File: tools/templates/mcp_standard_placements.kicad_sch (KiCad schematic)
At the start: 150 parts, among them J1 ICSP, J3 PIR BOARD, J5 MOTOR, J6 DNP, Q1 FMOS3401A?, Q11 MMBTA55?, Q2 BC847B?, Q3 MMBTA55?, Q4 MMBTA55?, Q5 MMBTA55?, Q6 MMBTA55?, Q7 BC857C?, Q8 N/P pair? (372A), Q9 DNP, U1 S-1200B45? [pins], U106 U6A / DNP, U2 SN74LVC2G14DBV?, U3 SGM8542XS, U4 PIC16F18855, U5 MX512H, U6 S-812C33AMC? / 3.3V, U7 DNP, Y1 20 MHz

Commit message: Record measured D3 rails and R42 continuity; close V082 association
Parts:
- D3: PhysicalConnectionEvidence (none) -> 2026-10-09 user meter report: D3.L=GND; D3.R=VDD TP via V08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
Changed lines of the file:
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@@
 				) hide)
 		)
+    (property "PhysicalConnectionEvidence" "2026-10-09 user meter report: D3.L=GND; D3.R=VDD TP via V082. D3.S to R42=1.2 ohm; resistor end not explicitly named. Photo selects R42.2 nearest D3; other end already mapped to TP4/PIC25. Fitted BAV99 identity and signal function remain candidates." (at 556.26 233.68 0)
+      (effects (font (size 1.27 1.27)) (hide yes))
+    )
 	)
 	(symbol

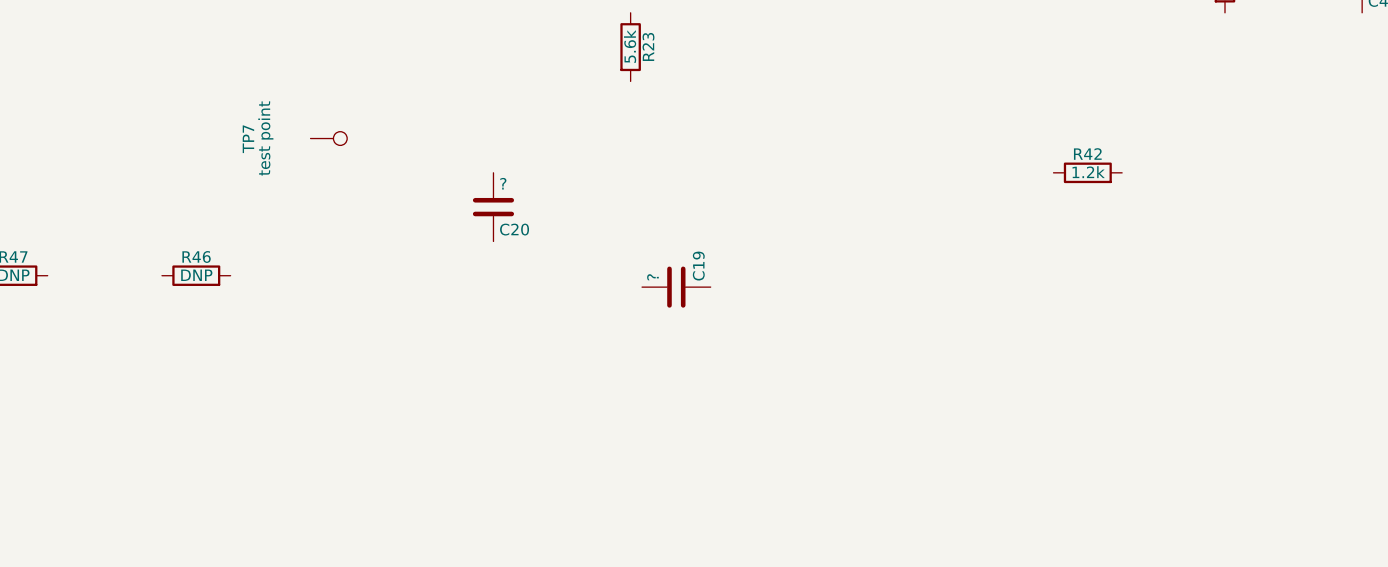
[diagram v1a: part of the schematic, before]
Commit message: Map D2 antenna and receiver connections with empty R46 option
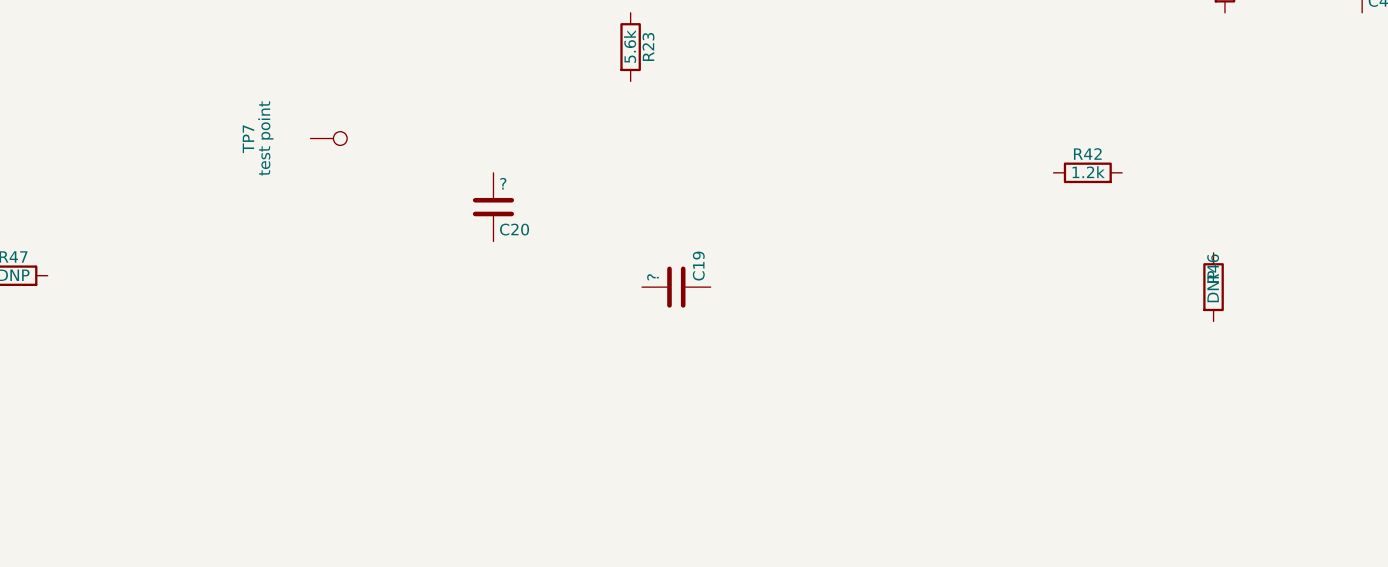
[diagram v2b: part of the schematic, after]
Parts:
- D2: MeasurementEvidence (none) -> User: R (upper-left)-C20 lower = 1 ohm; L (upper-right)-ANT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
- R46: MeasurementEvidence (none) -> User confirms empty R46 footprint: upper pad/model1 joins D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
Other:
- moved on the sheet: R46
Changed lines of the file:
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@@
 			)
 		)
-    (property "PhysicalPinEvidence" "IMG_2437 front: CLK-DAT-GND-VDD-VPP left to right; square pad is VPP/right end. IMG_2439 rear corroborates square end. Native pin1=VPP,2=VDD,3=GND,4=DAT,5=CLK; photo-based physical order, not new electrical measurements." (at 344.17 59.69 0)
-      (effects (font (size 1.27 1.27)) (hide yes))
-    )
+		(property "PhysicalPinEvidence" "IMG_2437 front: CLK-DAT-GND-VDD-VPP left to right; square pad is VPP/right end. IMG_2439 rear corroborates square end. Native pin1=VPP,2=VDD,3=GND,4=DAT,5=CLK; photo-based physical order, not new electrical measurements."
+			(at 344.17 59.69 0)
+			(effects
+				(font
+					(size 1.27 1.27)
+				)
+				(hide yes)
+			)
+		)
 		(pin "1"
 		)
@@
 	(symbol
 		(lib_id "Device:R")
-		(at 412.75 248.92 90)
+		(at 525.78 250.19 0)
 		(unit 1)
 		(body_style 1)
@@
 		(dnp no)
 		(property "Reference" "R46"
-			(at 412.75 246.888 90)
+			(at 525.78 248.15800000000002 90)
 			(show_name no)
 			(do_not_autoplace no)
@@
 		)
 		(property "Value" "DNP"
-			(at 412.75 248.92 90)
+			(at 525.78 250.19 90)
 			(show_name no)
 			(do_not_autoplace no)
@@
 		)
 		(property "Footprint" "Resistor_SMD:R_0603_1608Metric"
-			(at 412.75 250.698 90)
+			(at 525.78 251.96800000000002 90)
 			(hide yes)
 			(show_name no)
@@
 		)
 		(property "Datasheet" ""
-			(at 412.75 248.92 0)
+			(at 525.78 250.19 0)
 			(hide yes)
 			(show_name no)
@@
 		)
 		(property "Description" "Resistor"
-			(at 412.75 248.92 0)
+			(at 525.78 250.19 0)
 			(hide yes)
 			(show_name no)
@@
 			)
 		)
+    (property "MeasurementEvidence" "User confirms empty R46 footprint: upper pad/model1 joins D2.L/ANT2; lower pad/model2 joins D2.S. Remains DNP; no conducting bridge is fitted." (at 525.78 250.19 0)
+      (effects (font (size 1.27 1.27)) (hide yes))
+    )
 		(pin "1"
 		)
@@
 			)
 		)
+		(property "MeasurementEvidence" "User: R (upper-left)-C20 lower = 1 ohm; L (upper-right)-ANT2 and R46 upper directly connected; S (single lower)-R46 lower directly connected. R46 DNP, not a jumper. S-ANT2 OL; S-GND 700 kohm; S-VREF 1.32 Mohm. D2 L=1/R=2/S=3 are placeholder IDs; R46 upper=1/lower=2."
+			(at 556.26 251.46 0)
+			(effects
+				(font
+					(size 1.27 1.27)
+				)
+				(hide yes)
+			)
+		)
 		(pin "1"
 		)
@@
 				) hide)
 		)
-    (property "PhysicalConnectionEvidence" "2026-10-09 user meter report: D3.L=GND; D3.R=VDD TP via V082. D3.S to R42=1.2 ohm; resistor end not explicitly named. Photo selects R42.2 nearest D3; other end already mapped to TP4/PIC25. Fitted BAV99 identity and signal function remain candidates." (at 556.26 233.68 0)
-      (effects (font (size 1.27 1.27)) (hide yes))
-    )
+		(property "PhysicalConnectionEvidence" "2026-10-09 user meter report: D3.L=GND; D3.R=VDD TP via V082. D3.S to R42=1.2 ohm; resistor end not explicitly named. Photo selects R42.2 nearest D3; other end already mapped to TP4/PIC25. Fitted BAV99 identity and signal function remain candidates."
+			(at 556.26 233.68 0)
+			(effects
+				(font
+					(size 1.27 1.27)
+				)
+				(hide yes)
+			)
+		)
 	)
 	(symbol

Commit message: Resolve measured U3 bias and J3 ground; queue focused follow-up checks
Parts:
- J3: MeasurementEvidence (none) -> v0.9.13 user: pin3 (left / I in IMG_2435)-GND 1 ohm; pin2 (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; ViaEvidence v0.9.8: User confirms V067-J3 pin1 (red wire), on modeled H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 -> v0.9.13 user: pin3 (left / I in IMG_2435)-GND 1 ohm; pin2 (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
- R22: MeasurementEvidence (none) -> v0.9.13 user: D/left end in IMG_2434 is model2, U3.5/VREF a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; ViaEvidence v0.9.8: User confirms V071-VREF. Earlier V071-R21.2 and V02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 -> v0.9.13 user: D/left end in IMG_2434 is model2, U3.5/VREF a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
- R23: MeasurementEvidence (none) -> v0.9.13 user: both physical ends 270-289 kohm to U3.5, now 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; ViaEvidence v0.9.8: User confirms V071-VREF. Earlier V071-R21.2 and V02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 -> v0.9.13 user: both physical ends 270-289 kohm to U3.5, now 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
- U3: MeasurementEvidence (none) -> v0.9.13 user: pin5-VREF 1 ohm; pin5-R22 D/left 1 ohm, E/rig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
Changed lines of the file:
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@@
 			)
 		)
+    (property "MeasurementEvidence" "v0.9.13 user: pin5-VREF 1 ohm; pin5-R22 D/left 1 ohm, E/right 10 kohm; both R23 ends 270-289 kohm. Pin5 and V079/V080 now VREF. Original C18.1 fragment retained; TP6/C18.2 stays separate across C18." (at 381.0 200.66 0)
+      (effects (font (size 1.27 1.27)) (hide yes))
+    )
 		(pin "1"
 		)
@@
 			)
 		)
-		(property "ViaEvidence" "v0.9.8: User confirms V071-VREF. Earlier V071-R21.2 and V026-VREF-PIC21/RB0 associations retained. R21.2 joins VREF. Existing R22.2/R23.2/R48.2 receiver-bias branches remain prior photo/circuit hypotheses, not new measured connections. VREF remains separate from VDD and RC1/V053. No voltage or numeric resistance supplied."
+		(property "ViaEvidence" "v0.9.13 user: both physical ends 270-289 kohm to U3.5, now confirmed VREF. Withdraw R23.2-VREF; leave pad2 unresolved. Prior pad1-to-U3.6 feedback link and physical-end numbering remain hypotheses. Marked 562 nominal 5.6k retained."
 			(at 461.01 223.52 0)
 			(effects
 				(font
 					(size 1.27 1.27)
-				)
-				(hide yes)
-			)
+				) (hide yes))
 		)
+    (property "MeasurementEvidence" "v0.9.13 user: both physical ends 270-289 kohm to U3.5, now confirmed VREF. Withdraw R23.2-VREF; leave pad2 unresolved. Prior pad1-to-U3.6 feedback link and physical-end numbering remain hypotheses. Marked 562 nominal 5.6k retained." (at 461.01 223.52 0)
+      (effects (font (size 1.27 1.27)) (hide yes))
+    )
 		(pin "1"
 		)
@@
 			)
 		)
-		(property "ViaEvidence" "v0.9.8: User confirms V071-VREF. Earlier V071-R21.2 and V026-VREF-PIC21/RB0 associations retained. R21.2 joins VREF. Existing R22.2/R23.2/R48.2 receiver-bias branches remain prior photo/circuit hypotheses, not new measured connections. VREF remains separate from VDD and RC1/V053. No voltage or numeric resistance supplied."
+		(property "ViaEvidence" "v0.9.13 user: D/left end in IMG_2434 is model2, U3.5/VREF at 1 ohm. E/right/model1 is 10 kohm from U3.5. Marked 01C nominal 10k retained; E-to-GND is still a prior hypothesis awaiting direct check."
 			(at 326.39 229.87 0)
 			(effects
 				(font
 					(size 1.27 1.27)
-				)
-				(hide yes)
-			)
+				) (hide yes))
 		)
+    (property "MeasurementEvidence" "v0.9.13 user: D/left end in IMG_2434 is model2, U3.5/VREF at 1 ohm. E/right/model1 is 10 kohm from U3.5. Marked 01C nominal 10k retained; E-to-GND is still a prior hypothesis awaiting direct check." (at 326.39 229.87 0)
+      (effects (font (size 1.27 1.27)) (hide yes))
+    )
 		(pin "1"
 		)
@@
 			)
 		)
-		(property "ViaEvidence" "v0.9.8: User confirms V067-J3 pin1 (red wire), on modeled H_PIR_VDD. Prior V067-U6A.R1 local pad association retained. Empty U6A option remains DNP; this does not identify an IC or confirm every other H_PIR_VDD branch."
+		(property "ViaEvidence" "v0.9.13 user: pin3 (left / I in IMG_2435)-GND 1 ohm; pin2 (middle / H)-GND 290 kohm. Correct pin3 to GND, withdraw pin2 ground and pin3 raw-signal hypotheses. Pin1 supply remains confirmed. Pin2 destination awaits R38 checks."
 			(at 405.13 327.66 0)
 			(effects
 				(font
 					(size 1.27 1.27)
-				)
-				(hide yes)
-			)
+				) (hide yes))
 		)
+    (property "MeasurementEvidence" "v0.9.13 user: pin3 (left / I in IMG_2435)-GND 1 ohm; pin2 (middle / H)-GND 290 kohm. Correct pin3 to GND, withdraw pin2 ground and pin3 raw-signal hypotheses. Pin1 supply remains confirmed. Pin2 destination awaits R38 checks." (at 405.13 327.66 0)
+      (effects (font (size 1.27 1.27)) (hide yes))
+    )
 		(pin "1"
 		)

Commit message: Confirm J3 signal entry, R23 input and R22 ground from bench readings
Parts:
- J3: MeasurementEvidence v0.9.13 user: pin3 (left / I in IMG_2435)-GND 1 ohm; pin2 (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 -> v0.9.14 user: pin1 PIR supply previously confirmed; pin2 H-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; ViaEvidence v0.9.13 user: pin3 (left / I in IMG_2435)-GND 1 ohm; pin2 (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 -> v0.9.14 user: pin1 PIR supply previously confirmed; pin2 H-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
- R22: MeasurementEvidence v0.9.13 user: D/left end in IMG_2434 is model2, U3.5/VREF a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 -> v0.9.14 user: E/right/model1-GND 1 ohm; D/left/model2-VREF 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; ViaEvidence v0.9.13 user: D/left end in IMG_2434 is model2, U3.5/VREF a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 -> v0.9.14 user: E/right/model1-GND 1 ohm; D/left/model2-VREF 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
- R23: MeasurementEvidence v0.9.13 user: both physical ends 270-289 kohm to U3.5, now 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 -> v0.9.14 user: B/left/model1-U3.6 1 ohm; C/right/model2-U3.6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; ViaEvidence v0.9.13 user: both physical ends 270-289 kohm to U3.5, now 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 -> v0.9.14 user: B/left/model1-U3.6 1 ohm; C/right/model2-U3.6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
- R38: MeasurementEvidence (none) -> v0.9.14 user: K/right/model1-J3.2 1 ohm; J/left/model2-J3.2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
- U3: MeasurementEvidence v0.9.13 user: pin5-VREF 1 ohm; pin5-R22 D/left 1 ohm, E/rig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 -> v0.9.14 user: pin5-VREF/R22 D 1 ohm (batch1); pin6-R23 B/le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
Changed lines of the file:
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@@
 			)
 		)
-    (property "MeasurementEvidence" "v0.9.13 user: pin5-VREF 1 ohm; pin5-R22 D/left 1 ohm, E/right 10 kohm; both R23 ends 270-289 kohm. Pin5 and V079/V080 now VREF. Original C18.1 fragment retained; TP6/C18.2 stays separate across C18." (at 381.0 200.66 0)
+    (property "MeasurementEvidence" "v0.9.14 user: pin5-VREF/R22 D 1 ohm (batch1); pin6-R23 B/left/model1 1 ohm and C/right/model2 5.6 kohm. Pin6-R22 E/GND 400 kohm. Pin5 and pin6 remain distinct; C18 branch is retained photo evidence, not meter-confirmed." (at 381.0 200.66 0)
       (effects (font (size 1.27 1.27)) (hide yes))
     )
@@
 			)
 		)
-		(property "ViaEvidence" "v0.9.13 user: both physical ends 270-289 kohm to U3.5, now confirmed VREF. Withdraw R23.2-VREF; leave pad2 unresolved. Prior pad1-to-U3.6 feedback link and physical-end numbering remain hypotheses. Marked 562 nominal 5.6k retained."
+		(property "ViaEvidence" "v0.9.14 user: B/left/model1-U3.6 1 ohm; C/right/model2-U3.6 5.6 kohm, agreeing with 562 marking. C destination remains open; earlier VREF guess rejected by 270-289 kohm to pin5. Pin6-GND 400 kohm also rejects a direct pin6-ground join."
 			(at 461.01 223.52 0)
 			(effects
@@
 				) (hide yes))
 		)
-    (property "MeasurementEvidence" "v0.9.13 user: both physical ends 270-289 kohm to U3.5, now confirmed VREF. Withdraw R23.2-VREF; leave pad2 unresolved. Prior pad1-to-U3.6 feedback link and physical-end numbering remain hypotheses. Marked 562 nominal 5.6k retained." (at 461.01 223.52 0)
+    (property "MeasurementEvidence" "v0.9.14 user: B/left/model1-U3.6 1 ohm; C/right/model2-U3.6 5.6 kohm, agreeing with 562 marking. C destination remains open; earlier VREF guess rejected by 270-289 kohm to pin5. Pin6-GND 400 kohm also rejects a direct pin6-ground join." (at 461.01 223.52 0)
       (effects (font (size 1.27 1.27)) (hide yes))
     )
@@
 			)
 		)
-		(property "ViaEvidence" "v0.9.13 user: D/left end in IMG_2434 is model2, U3.5/VREF at 1 ohm. E/right/model1 is 10 kohm from U3.5. Marked 01C nominal 10k retained; E-to-GND is still a prior hypothesis awaiting direct check."
+		(property "ViaEvidence" "v0.9.14 user: E/right/model1-GND 1 ohm; D/left/model2-VREF confirmed in batch1. R22 spans VREF to GND; 10 kohm agrees with 01C marking. U3 pin6 to E is 400 kohm and is not a wire."
 			(at 326.39 229.87 0)
 			(effects
@@
 				) (hide yes))
 		)
-    (property "MeasurementEvidence" "v0.9.13 user: D/left end in IMG_2434 is model2, U3.5/VREF at 1 ohm. E/right/model1 is 10 kohm from U3.5. Marked 01C nominal 10k retained; E-to-GND is still a prior hypothesis awaiting direct check." (at 326.39 229.87 0)
+    (property "MeasurementEvidence" "v0.9.14 user: E/right/model1-GND 1 ohm; D/left/model2-VREF confirmed in batch1. R22 spans VREF to GND; 10 kohm agrees with 01C marking. U3 pin6 to E is 400 kohm and is not a wire." (at 326.39 229.87 0)
       (effects (font (size 1.27 1.27)) (hide yes))
     )
@@
 			)
 		)
-		(property "ViaEvidence" "v0.9.13 user: pin3 (left / I in IMG_2435)-GND 1 ohm; pin2 (middle / H)-GND 290 kohm. Correct pin3 to GND, withdraw pin2 ground and pin3 raw-signal hypotheses. Pin1 supply remains confirmed. Pin2 destination awaits R38 checks."
+		(property "ViaEvidence" "v0.9.14 user: pin1 PIR supply previously confirmed; pin2 H-R38 K/right/model1 1 ohm and H-R38 J/left/model2 10 kohm; pin3-GND 1 ohm. Pin2-GND remains 290 kohm (batch1), distinct from ground. Q2 onward/controller route remains unverified."
 			(at 405.13 327.66 0)
 			(effects
@@
 				) (hide yes))
 		)
-    (property "MeasurementEvidence" "v0.9.13 user: pin3 (left / I in IMG_2435)-GND 1 ohm; pin2 (middle / H)-GND 290 kohm. Correct pin3 to GND, withdraw pin2 ground and pin3 raw-signal hypotheses. Pin1 supply remains confirmed. Pin2 destination awaits R38 checks." (at 405.13 327.66 0)
+    (property "MeasurementEvidence" "v0.9.14 user: pin1 PIR supply previously confirmed; pin2 H-R38 K/right/model1 1 ohm and H-R38 J/left/model2 10 kohm; pin3-GND 1 ohm. Pin2-GND remains 290 kohm (batch1), distinct from ground. Q2 onward/controller route remains unverified." (at 405.13 327.66 0)
       (effects (font (size 1.27 1.27)) (hide yes))
     )
@@
 			)
 		)
+    (property "MeasurementEvidence" "v0.9.14 user: K/right/model1-J3.2 1 ohm; J/left/model2-J3.2 10 kohm, agreeing with 01C marking. Q2/R39 and R33 branches remain prior hypotheses beyond this measured pair." (at 341.63 345.44 0)
+      (effects (font (size 1.27 1.27)) (hide yes))
+    )
 		(pin "1"
 		)
